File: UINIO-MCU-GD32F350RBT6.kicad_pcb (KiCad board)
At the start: 2 copper layers, 88.1 x 25.4 mm, 36 parts, among them J1 Conn_01x32_Pin, J2 Conn_01x32_Pin, J3 Conn_01x04_Pin, SW1 BOOT0, SW2 NRST, U1 ME6211C33M5G-N, U2 GD32F350RBT6, Y1 32.768KHz, Y2 8MHz

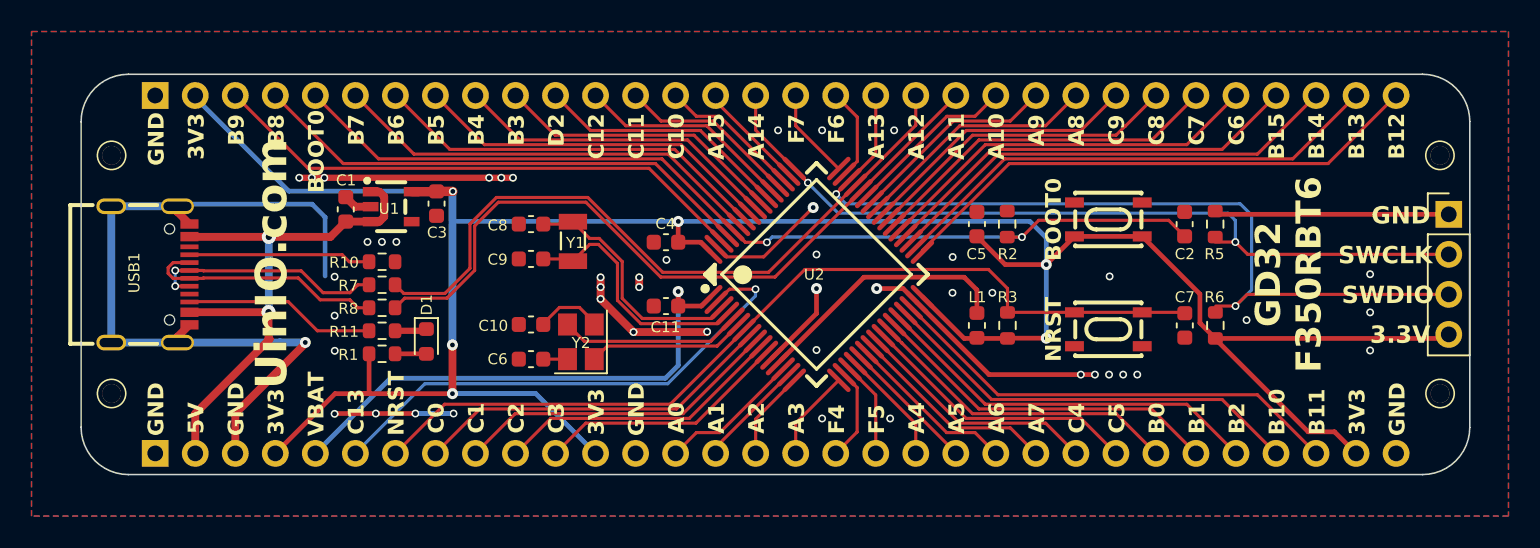
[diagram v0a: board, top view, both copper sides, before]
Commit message: Release UINIO-MCU-GD32F350RBT6 version 3.3.0.
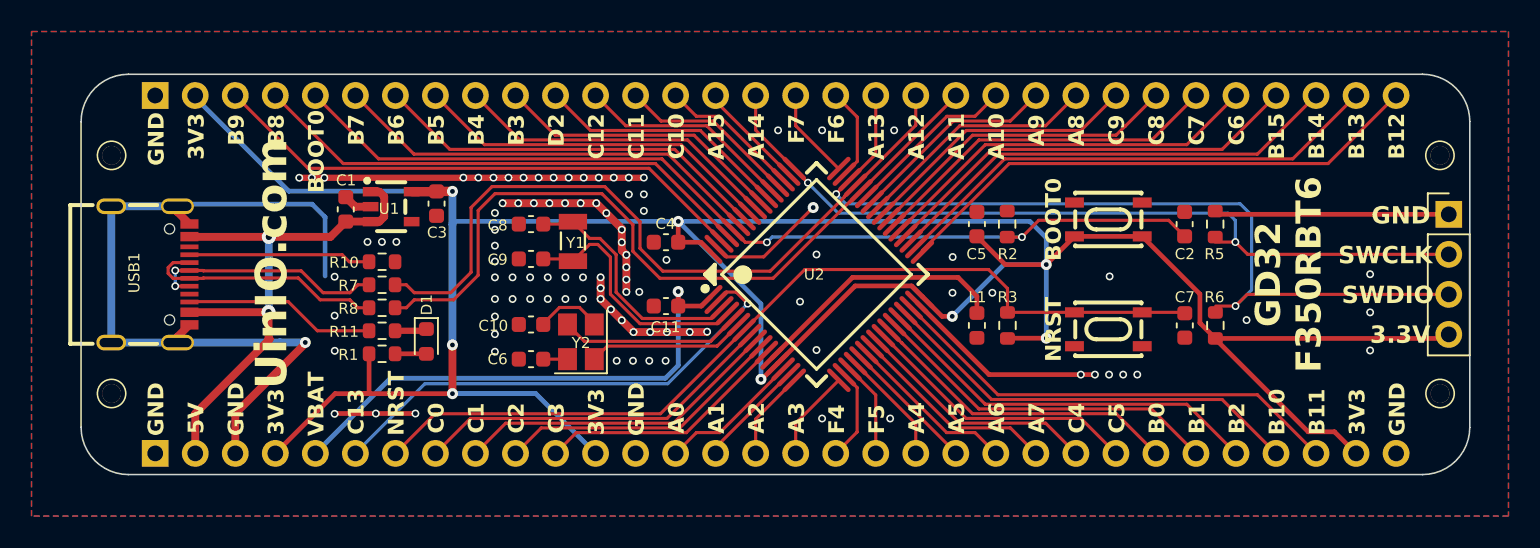
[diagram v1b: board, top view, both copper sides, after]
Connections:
- net /PA11 renamed /USB_PA-
- net /PA12 renamed /USB_PA+
- L1 pad 1: /VDD_3.3V -> GND
- L1 pad 2: Net-(U2-VDDA) -> /VSSA
- U2 pad 12: GND -> /VSSA
- U2 pad 13: Net-(U2-VDDA) -> /VDD_3.3V
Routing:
- net /VDD_3.3V: track 166.4 -> 193.0 mm, vias 6 -> 8
- net /VSSA: track 0.00 -> 16.7 mm
- net Net-(U2-VDDA): track 16.1 -> 0.00 mm
- net GND: track 129.0 -> 138.1 mm, vias 48 -> 100
- net /USB_PA-: track 46.7 -> 49.0 mm
- net /USB_PA+: track 45.2 -> 47.4 mm
- net /PC13: track 32.8 -> 31.4 mm
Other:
- board text added: "Version 3.3.0"
- board text removed: "Version 3.2.0"

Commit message: Release UINIO-MCU-GD32F350RBT6 version 3.3.0.
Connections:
- net /USB_PA+ renamed /PA12
- net /USB_PA- renamed /PA11
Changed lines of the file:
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@@
   (net 69 "Net-(USB1-CC2)")
   (net 70 "unconnected-(USB1-SBU2-PadB8)")
-  (net 71 "/USB_PA+")
-  (net 72 "/USB_PA-")
+  (net 71 "/PA12")
+  (net 72 "/PA11")
   (footprint "Resistor_SMD:R_0603_1608Metric" (layer "F.Cu")
     (at 178.36 100.44 -90)
@@
       (net 50 "/PA10") (pinfunction "PA10") (pintype "input"))
     (pad "44" smd oval (at -1.75 -5.75 315) (size 0.3 2) (layers "F.Cu" "F.Paste" "F.Mask")
-      (net 72 "/USB_PA-") (pinfunction "PA11") (pintype "input"))
+      (net 72 "/PA11") (pinfunction "PA11") (pintype "input"))
     (pad "45" smd oval (at -2.25 -5.75 315) (size 0.3 2) (layers "F.Cu" "F.Paste" "F.Mask")
-      (net 71 "/USB_PA+") (pinfunction "PA12") (pintype "input"))
+      (net 71 "/PA12") (pinfunction "PA12") (pintype "input"))
     (pad "46" smd oval (at -2.75 -5.75 315) (size 0.3 2) (layers "F.Cu" "F.Paste" "F.Mask")
       (net 49 "/PA13{slash}SWDIO") (pinfunction "PA13") (pintype "input"))
@@
       (stroke (width 0.1) (type solid)) (layer "F.Fab"))
     (pad "1" smd roundrect (at -0.825 0 180) (size 0.8 0.95) (layers "F.Cu" "F.Paste" "F.Mask") (roundrect_rratio 0.25)
-      (net 71 "/USB_PA+") (pintype "passive"))
+      (net 71 "/PA12") (pintype "passive"))
     (pad "2" smd roundrect (at 0.825 0 180) (size 0.8 0.95) (layers "F.Cu" "F.Paste" "F.Mask") (roundrect_rratio 0.25)
       (net 66 "/USB_Data+") (pintype "passive"))
@@
       (stroke (width 0.1) (type solid)) (layer "F.Fab"))
     (pad "1" smd roundrect (at -0.825 0 180) (size 0.8 0.95) (layers "F.Cu" "F.Paste" "F.Mask") (roundrect_rratio 0.25)
-      (net 72 "/USB_PA-") (pintype "passive"))
+      (net 72 "/PA11") (pintype "passive"))
     (pad "2" smd roundrect (at 0.825 0 180) (size 0.8 0.95) (layers "F.Cu" "F.Paste" "F.Mask") (roundrect_rratio 0.25)
       (net 67 "/USB_Data-") (pintype "passive"))
@@
       (net 49 "/PA13{slash}SWDIO") (pinfunction "Pin_19") (pintype "passive"))
     (pad "20" thru_hole oval (at 0 -48.26 270) (size 1.7 1.7) (drill 1) (layers "*.Cu" "*.Mask")
-      (net 71 "/USB_PA+") (pinfunction "Pin_20") (pintype "passive"))
+      (net 71 "/PA12") (pinfunction "Pin_20") (pintype "passive"))
     (pad "21" thru_hole oval (at 0 -50.8 270) (size 1.7 1.7) (drill 1) (layers "*.Cu" "*.Mask")
-      (net 72 "/USB_PA-") (pinfunction "Pin_21") (pintype "passive"))
+      (net 72 "/PA11") (pinfunction "Pin_21") (pintype "passive"))
     (pad "22" thru_hole oval (at 0 -53.34 270) (size 1.7 1.7) (drill 1) (layers "*.Cu" "*.Mask")
       (net 50 "/PA10") (pinfunction "Pin_22") (pintype "passive"))
@@
     )
   )
-  (zone (net 72) (net_name "/USB_PA-") (layer "F.Cu") (name "$teardrop_padvia$") (hatch edge 0.5)
+  (zone (net 72) (net_name "/PA11") (layer "F.Cu") (name "$teardrop_padvia$") (hatch edge 0.5)
     (priority 30106)
     (attr (teardrop (type padvia)))
@@
     )
   )
-  (zone (net 71) (net_name "/USB_PA+") (layer "F.Cu") (name "$teardrop_padvia$") (hatch edge 0.5)
+  (zone (net 71) (net_name "/PA12") (layer "F.Cu") (name "$teardrop_padvia$") (hatch edge 0.5)
     (priority 30003)
     (attr (teardrop (type padvia)))
@@
     )
   )
-  (zone (net 71) (net_name "/USB_PA+") (layer "F.Cu") (name "$teardrop_padvia$") (hatch edge 0.5)
+  (zone (net 71) (net_name "/PA12") (layer "F.Cu") (name "$teardrop_padvia$") (hatch edge 0.5)
     (priority 30177)
     (attr (teardrop (type padvia)))
@@
     )
   )
-  (zone (net 71) (net_name "/USB_PA+") (layer "F.Cu") (name "$teardrop_padvia$") (hatch edge 0.5)
+  (zone (net 71) (net_name "/PA12") (layer "F.Cu") (name "$teardrop_padvia$") (hatch edge 0.5)
     (priority 30104)
     (attr (teardrop (type padvia)))
@@
     )
   )
-  (zone (net 72) (net_name "/USB_PA-") (layer "F.Cu") (name "$teardrop_padvia$") (hatch edge 0.5)
+  (zone (net 72) (net_name "/PA11") (layer "F.Cu") (name "$teardrop_padvia$") (hatch edge 0.5)
     (priority 30054)
     (attr (teardrop (type padvia)))
@@
     )
   )
-  (zone (net 72) (net_name "/USB_PA-") (layer "F.Cu") (name "$teardrop_padvia$") (hatch edge 0.5)
+  (zone (net 72) (net_name "/PA11") (layer "F.Cu") (name "$teardrop_padvia$") (hatch edge 0.5)
     (priority 30167)
     (attr (teardrop (type padvia)))

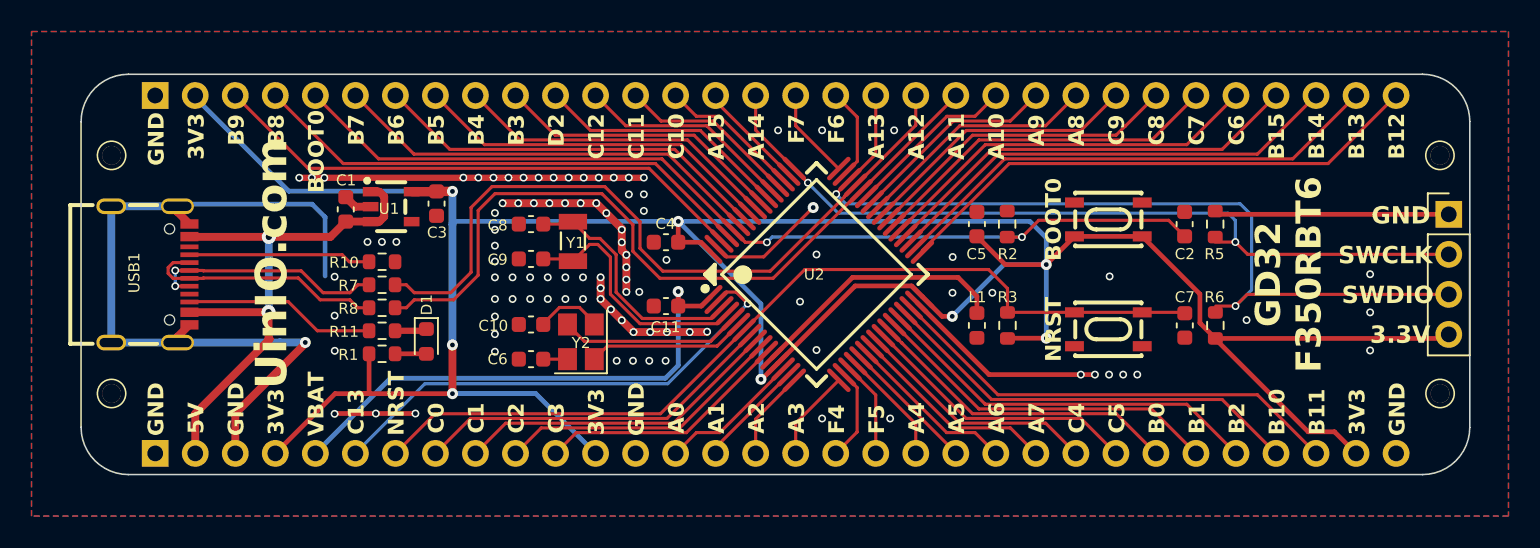
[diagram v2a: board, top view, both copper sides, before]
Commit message: Release UINIO-MCU-GD32F350RBT6 version 3.3.0.
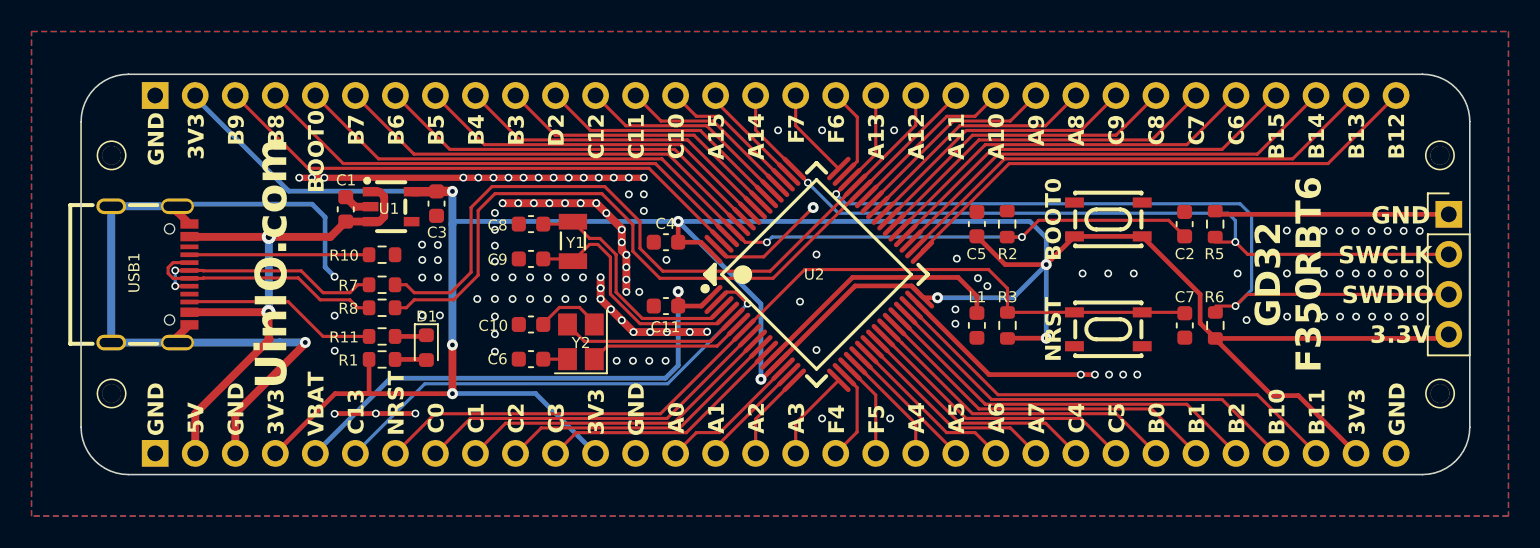
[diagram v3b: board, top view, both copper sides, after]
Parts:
- moved R10 0.45 mm to (125.5, 102.4)
- moved D1 0.39 mm to (128.3, 108.3)
- moved R11 0.36 mm to (125.5, 107.6)
- moved R1 0.36 mm to (125.5, 109.0)
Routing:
- net /VDD_3.3V: track 193.0 -> 191.6 mm
- net GND: track 138.1 -> 138.4 mm, vias 100 -> 132
